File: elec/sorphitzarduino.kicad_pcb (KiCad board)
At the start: 2 copper layers, 135.9 x 67.3 mm, 13 parts, among them J1 9V_BATT, J2 SWITCH, J3 AUDIO_JACK, U1 ARDUINO_MICRO_SHIELD

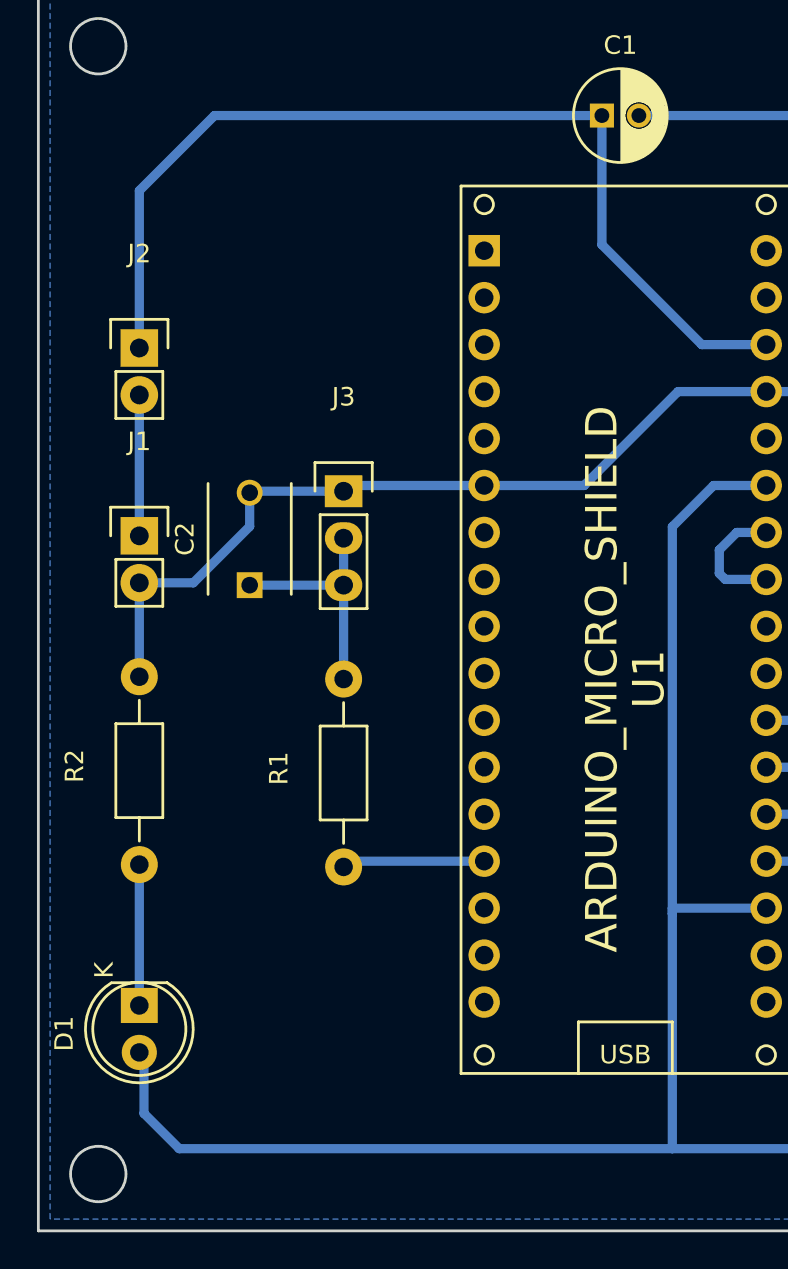
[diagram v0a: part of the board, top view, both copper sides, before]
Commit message: Upating to HIFI output circuit, and adding sontrol of LED
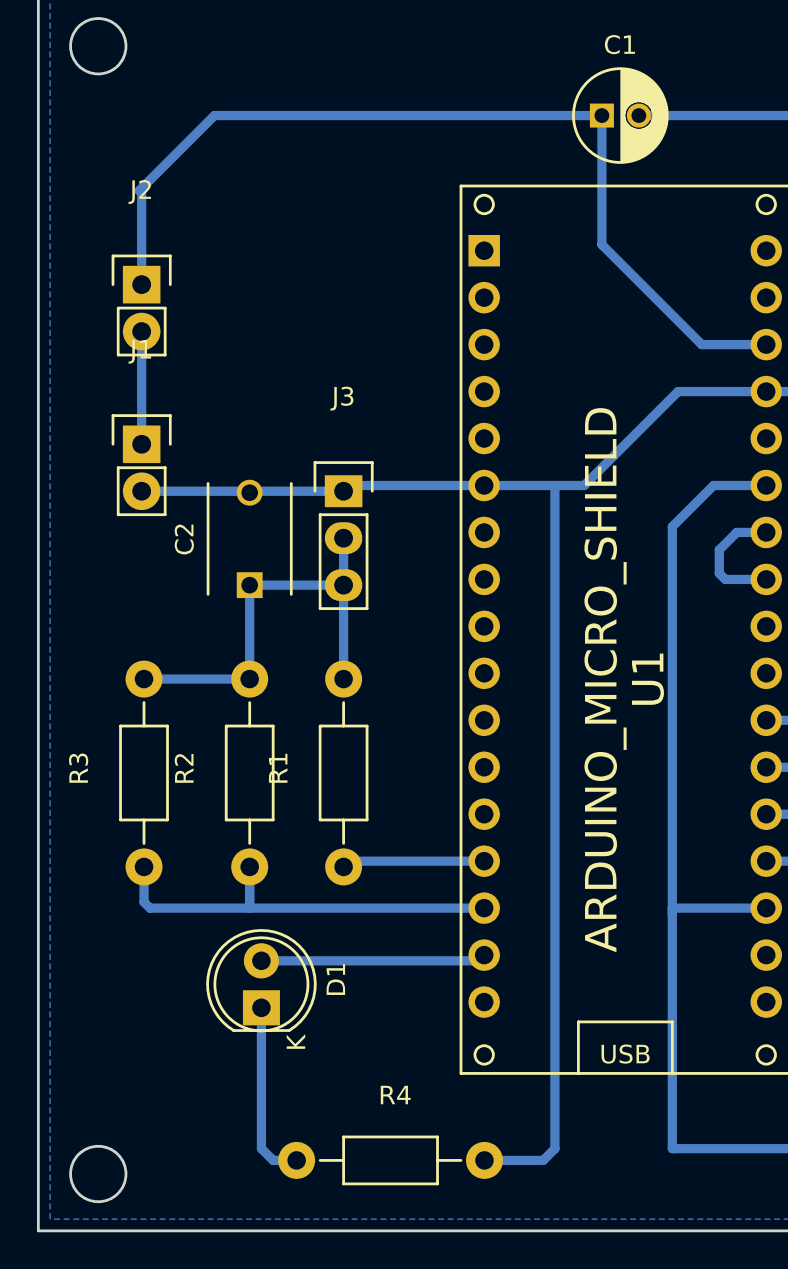
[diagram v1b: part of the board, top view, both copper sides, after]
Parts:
- added R3: 1M, Resistors_ThroughHole:Resistor_Horizontal_RM10mm, F.Cu at (117.5, 72.4)
- added R4: 290, Resistors_ThroughHole:Resistor_Horizontal_RM10mm, F.Cu at (125.7, 88.3)
- C2: value 100n -> 4.7nF
- R1: value 270 -> 3.9k
- R2: value 290 -> 1M
- moved D1 6.61 mm to (123.8, 80.0), turned to 90 degrees
- moved R2 5.97 mm to (123.2, 72.4)
- moved J1 4.95 mm to (117.3, 49.5)
- moved J2 3.43 mm to (117.3, 40.9)
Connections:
- D1 pad 2: +5V -> Net-(D1-Pad2)
- R2 pad 1: Net-(D1-Pad1) -> Net-(R2-Pad1)
- R2 pad 2: GND -> Net-(C2-Pad1)
- U1 pad 10: Net-(U1-Pad10) -> Net-(R2-Pad1)
- U1 pad 11: Net-(U1-Pad11) -> Net-(D1-Pad2)
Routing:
- net +5V: track 237.5 -> 204.8 mm
- net GND: track 152.0 -> 183.7 mm
- net Net-(R2-Pad1): track 0.00 -> 24.6 mm
- net Net-(D1-Pad2): track 0.00 -> 12.2 mm
- net Net-(C2-Pad1): track 12.7 -> 23.5 mm
- net Net-(C1-Pad1): track 53.3 -> 50.2 mm
- net Net-(D1-Pad1): track 7.62 -> 9.79 mm
- net Net-(J1-Pad1): track 7.62 -> 6.10 mm
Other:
- net class Default: clearance 0.2 -> 0.4
- rule trace_clearance: 0.2 -> 0.4

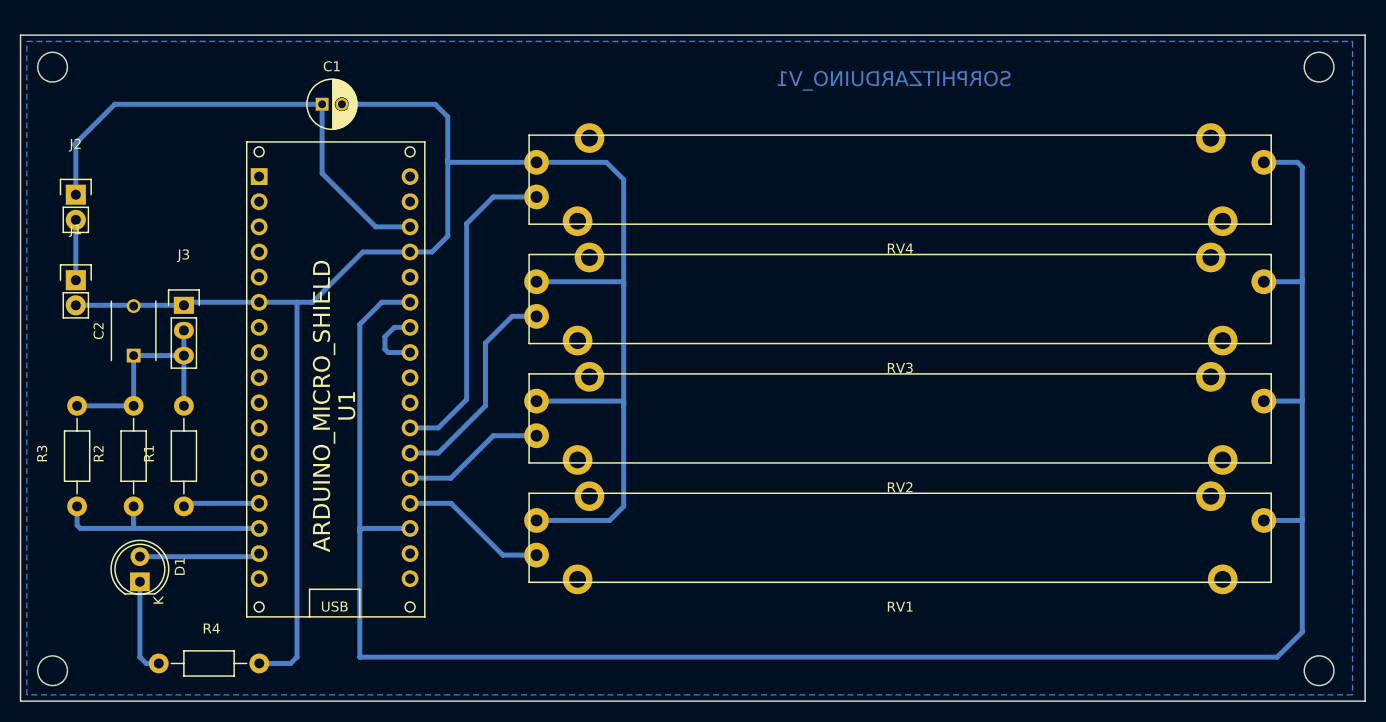
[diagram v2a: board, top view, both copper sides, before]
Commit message: Generating better PNG files for milling
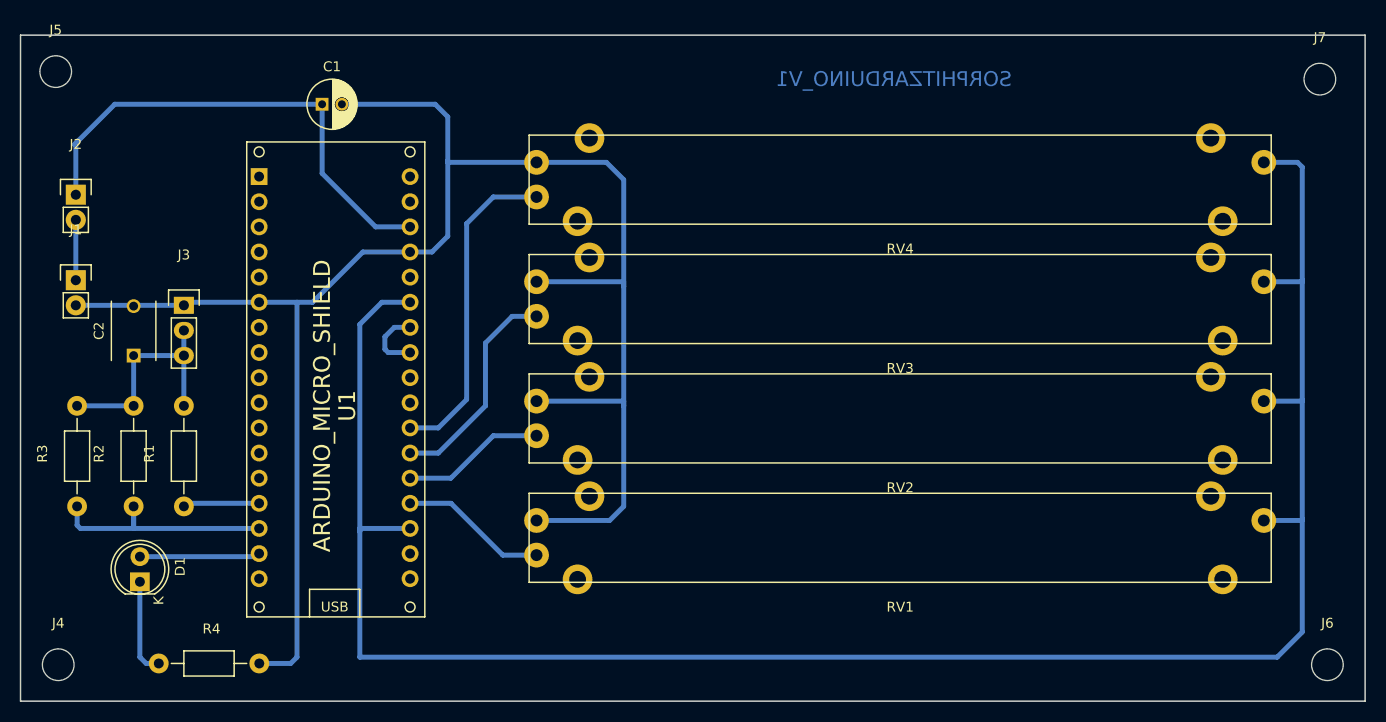
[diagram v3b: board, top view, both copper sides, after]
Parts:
- added J4: Mounting Hole, MountingHole:MountingHole_3.2mm_M3, F.Cu at (115.6, 88.4)
- added J5: Mounting Hole, MountingHole:MountingHole_3.2mm_M3, F.Cu at (115.3, 28.4)
- added J6: Mounting Hole, MountingHole:MountingHole_3.2mm_M3, F.Cu at (243.8, 88.4)
- added J7: Mounting Hole, MountingHole:MountingHole_3.2mm_M3, F.Cu at (243.1, 29.2)
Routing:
- removed copper zone on B.Cu, net GND
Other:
- outline, holes or cut-outs redrawn
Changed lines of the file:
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@@
-(kicad_pcb (version 20171130) (host pcbnew 5.0.1-33cea8e~68~ubuntu18.04.1)
+(kicad_pcb (version 20171130) (host pcbnew 5.0.2-bee76a0~70~ubuntu16.04.1)
   (general
     (thickness 1.6)
-    (drawings 11)
+    (drawings 7)
     (tracks 101)
     (zones 0)
-    (modules 15)
-    (nets 34)
+    (modules 19)
+    (nets 37)
   )
   (page A4)
@@
   )
   (layers
-    (0 F.Cu signal)
+    (0 F.Cu signal hide)
     (31 B.Cu signal)
-    (32 B.Adhes user)
-    (33 F.Adhes user)
-    (34 B.Paste user)
-    (35 F.Paste user)
-    (36 B.SilkS user)
-    (37 F.SilkS user)
+    (32 B.Adhes user hide)
+    (33 F.Adhes user hide)
+    (34 B.Paste user hide)
+    (35 F.Paste user hide)
+    (36 B.SilkS user hide)
+    (37 F.SilkS user hide)
     (38 B.Mask user)
-    (39 F.Mask user)
-    (40 Dwgs.User user)
-    (41 Cmts.User user)
-    (42 Eco1.User user)
-    (43 Eco2.User user)
+    (39 F.Mask user hide)
+    (40 Dwgs.User user hide)
+    (41 Cmts.User user hide)
+    (42 Eco1.User user hide)
+    (43 Eco2.User user hide)
     (44 Edge.Cuts user)
     (45 Margin user hide)
-    (46 B.CrtYd user)
-    (47 F.CrtYd user)
-    (48 B.Fab user)
-    (49 F.Fab user)
+    (46 B.CrtYd user hide)
+    (47 F.CrtYd user hide)
+    (48 B.Fab user hide)
+    (49 F.Fab user hide)
   )
   (setup
@@
     (mod_text_size 1 1)
     (mod_text_width 0.15)
-    (pad_size 1.524 1.524)
-    (pad_drill 0.762)
+    (pad_size 3.2 3.2)
+    (pad_drill 3.2)
     (pad_to_mask_clearance 0.2)
     (solder_mask_min_width 0.25)
@@
       (drillshape 1)
       (scaleselection 1)
-      (outputdirectory "Sorphitzarduino_Edge"))
+      (outputdirectory "holes"))
   )
   (net 0 "")
@@
   (net 32 "Net-(D1-Pad2)")
   (net 33 "Net-(R2-Pad1)")
+  (net 34 "Net-(J4-Pad1)")
+  (net 35 "Net-(J5-Pad1)")
+  (net 36 "Net-(J6-Pad1)")
   (net_class Default "This is the default net class."
     (clearance 0.4)
@@
     (add_net "Net-(D1-Pad2)")
     (add_net "Net-(J1-Pad1)")
+    (add_net "Net-(J4-Pad1)")
+    (add_net "Net-(J5-Pad1)")
+    (add_net "Net-(J6-Pad1)")
     (add_net "Net-(R1-Pad1)")
     (add_net "Net-(R2-Pad1)")
@@
     )
   )
+  (module MountingHole:MountingHole_3.2mm_M3 (layer F.Cu)
+    (at 115.57 88.392)
+    (descr "Mounting Hole 3.2mm, no annular, M3")
+    (tags "mounting hole 3.2mm no annular m3")
+    (attr virtual)
+    (fp_text reference J4 (at 0 -4.2) (layer F.SilkS)
+      (effects (font (size 1 1) (thickness 0.15)))
+    )
+    (fp_text value "Mounting Hole" (at 0 4.2) (layer F.Fab)
+      (effects (font (size 1 1) (thickness 0.15)))
+    )
+    (fp_circle (center 0 0) (end 3.45 0) (layer F.CrtYd) (width 0.05))
+    (fp_circle (center 0 0) (end 3.2 0) (layer Cmts.User) (width 0.15))
+    (fp_text user %R (at 0.3 0) (layer F.Fab)
+      (effects (font (size 1 1) (thickness 0.15)))
+    )
+    (pad 1 np_thru_hole circle (at 0 0) (size 3.2 3.2) (drill 3.2) (layers *.Cu *.Mask)
+      (net 34 "Net-(J4-Pad1)"))
+  )
+  (module MountingHole:MountingHole_3.2mm_M3 (layer F.Cu)
+    (at 115.316 28.448)
+    (descr "Mounting Hole 3.2mm, no annular, M3")
+    (tags "mounting hole 3.2mm no annular m3")
+    (attr virtual)
+    (fp_text reference J5 (at 0 -4.2) (layer F.SilkS)
+      (effects (font (size 1 1) (thickness 0.15)))
+    )
+    (fp_text value "Mounting Hole" (at 0 4.2) (layer F.Fab)
+      (effects (font (size 1 1) (thickness 0.15)))
+    )
+    (fp_text user %R (at 0.3 0) (layer F.Fab)
+      (effects (font (size 1 1) (thickness 0.15)))
+    )
+    (fp_circle (center 0 0) (end 3.2 0) (layer Cmts.User) (width 0.15))
+    (fp_circle (center 0 0) (end 3.45 0) (layer F.CrtYd) (width 0.05))
+    (pad 1 np_thru_hole circle (at 0 0) (size 3.2 3.2) (drill 3.2) (layers *.Cu *.Mask)
+      (net 35 "Net-(J5-Pad1)"))
+  )
+  (module MountingHole:MountingHole_3.2mm_M3 (layer F.Cu)
+    (at 243.84 88.392)
+    (descr "Mounting Hole 3.2mm, no annular, M3")
+    (tags "mounting hole 3.2mm no annular m3")
+    (attr virtual)
+    (fp_text reference J6 (at 0 -4.2) (layer F.SilkS)
+      (effects (font (size 1 1) (thickness 0.15)))
+    )
+    (fp_text value "Mounting Hole" (at 0 4.2) (layer F.Fab)
+      (effects (font (size 1 1) (thickness 0.15)))
+    )
+    (fp_circle (center 0 0) (end 3.45 0) (layer F.CrtYd) (width 0.05))
+    (fp_circle (center 0 0) (end 3.2 0) (layer Cmts.User) (width 0.15))
+    (fp_text user %R (at 0.3 0) (layer F.Fab)
+      (effects (font (size 1 1) (thickness 0.15)))
+    )
+    (pad 1 np_thru_hole circle (at 0 0) (size 3.2 3.2) (drill 3.2) (layers *.Cu *.Mask)
+      (net 36 "Net-(J6-Pad1)"))
+  )
+  (module MountingHole:MountingHole_3.2mm_M3 (layer F.Cu)
+    (at 243.078 29.21)
+    (descr "Mounting Hole 3.2mm, no annular, M3")
+    (tags "mounting hole 3.2mm no annular m3")
+    (attr virtual)
+    (fp_text reference J7 (at 0 -4.2) (layer F.SilkS)
+      (effects (font (size 1 1) (thickness 0.15)))
+    )
+    (fp_text value "Mounting Hole" (at 0 4.2) (layer F.Fab)
+      (effects (font (size 1 1) (thickness 0.15)))
+    )
+    (fp_text user %R (at 0.3 0) (layer F.Fab)
+      (effects (font (size 1 1) (thickness 0.15)))
+    )
+    (fp_circle (center 0 0) (end 3.2 0) (layer Cmts.User) (width 0.15))
+    (fp_circle (center 0 0) (end 3.45 0) (layer F.CrtYd) (width 0.05))
+    (pad "" np_thru_hole circle (at 0 0) (size 3.2 3.2) (drill 3.2) (layers *.Cu *.Mask))
+  )
   (gr_text SORPHITZARDUINO_V1 (at 200.025 29.21) (layer B.Cu)
     (effects (font (size 1.5 1.5) (thickness 0.3)) (justify mirror))
@@
     (arrow2b (pts (xy 220.345 34.925) (xy 219.758579 33.798496)))
   )
-  (gr_circle (center 115 89) (end 115 90.5) (layer Edge.Cuts) (width 0.15))
-  (gr_circle (center 115 28) (end 115 29.5) (layer Edge.Cuts) (width 0.15))
-  (gr_circle (center 243 89) (end 243 90.5) (layer Edge.Cuts) (width 0.15))
-  (gr_circle (center 243 28) (end 243 29.5) (layer Edge.Cuts) (width 0.15))
   (gr_line (start 111.76 92.075) (end 111.76 24.765) (angle 90) (layer Edge.Cuts) (width 0.15))
   (gr_line (start 247.65 92.075) (end 111.76 92.075) (angle 90) (layer Edge.Cuts) (width 0.15))
@@
   (segment (start 117.475 74.295) (end 117.475 72.39) (width 0.5) (layer B.Cu) (net 33))
   (segment (start 117.8 74.62) (end 117.475 74.295) (width 0.5) (layer B.Cu) (net 33))
-  (zone (net 2) (net_name GND) (layer B.Cu) (hatch edge 0.508)
-    (connect_pads (clearance 0.508))
-    (min_thickness 0.254)
-    (fill yes (arc_segments 16) (thermal_gap 0.508) (thermal_bridge_width 0.508))
-    (polygon
-      (pts
-        (xy 246.38 91.44) (xy 112.395 91.44) (xy 112.395 25.4) (xy 246.38 25.4) (xy 246.38 91.44)
-      )
-    )
-  )
 )
